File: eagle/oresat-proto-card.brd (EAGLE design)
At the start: 99 x 95.3 mm, 99 parts, among them J1 J-SAMTEC-TFM-110-X1-XXX-D-RA, J2 U.FL, J3 U.FL, J4 U.FL, J6 J-SAMTEC-TFM-120-X1-XXX-D-RA, J7 1.27MM-SWD-CONNECTOR, Q3 MOSFET-PCH-SOT23-6, Q4 MOSFET-PCH-SOT23-6, Q5 PMV45EN, Q6 PMV45EN, U2 TCAN330, U3 MAX7310, U4 MAX4211, U5 TPS62111, U6 STM32F042K6, X1 16MHZ-2.5x2mm

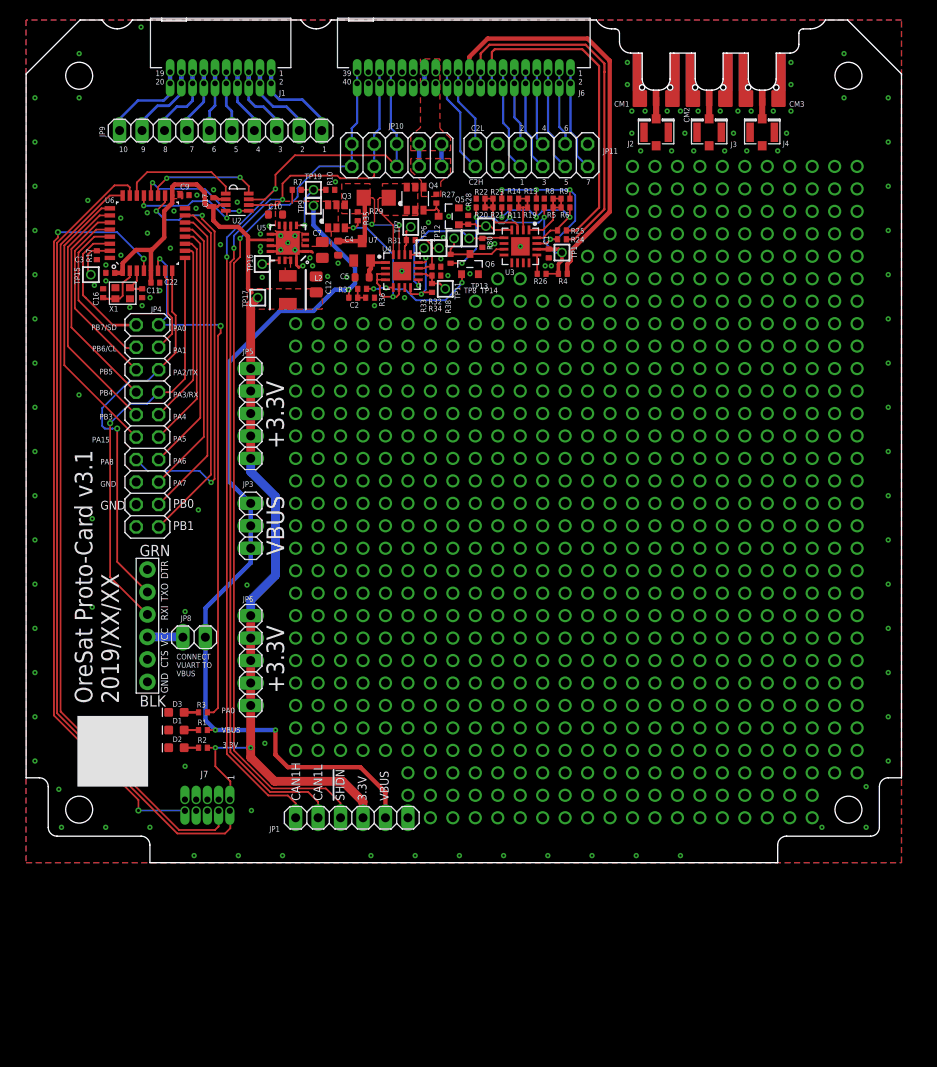
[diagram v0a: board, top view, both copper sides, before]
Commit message: More schematic and board polishing. Went over ERCs and DRCs, some layout polishing, more ground stitching.
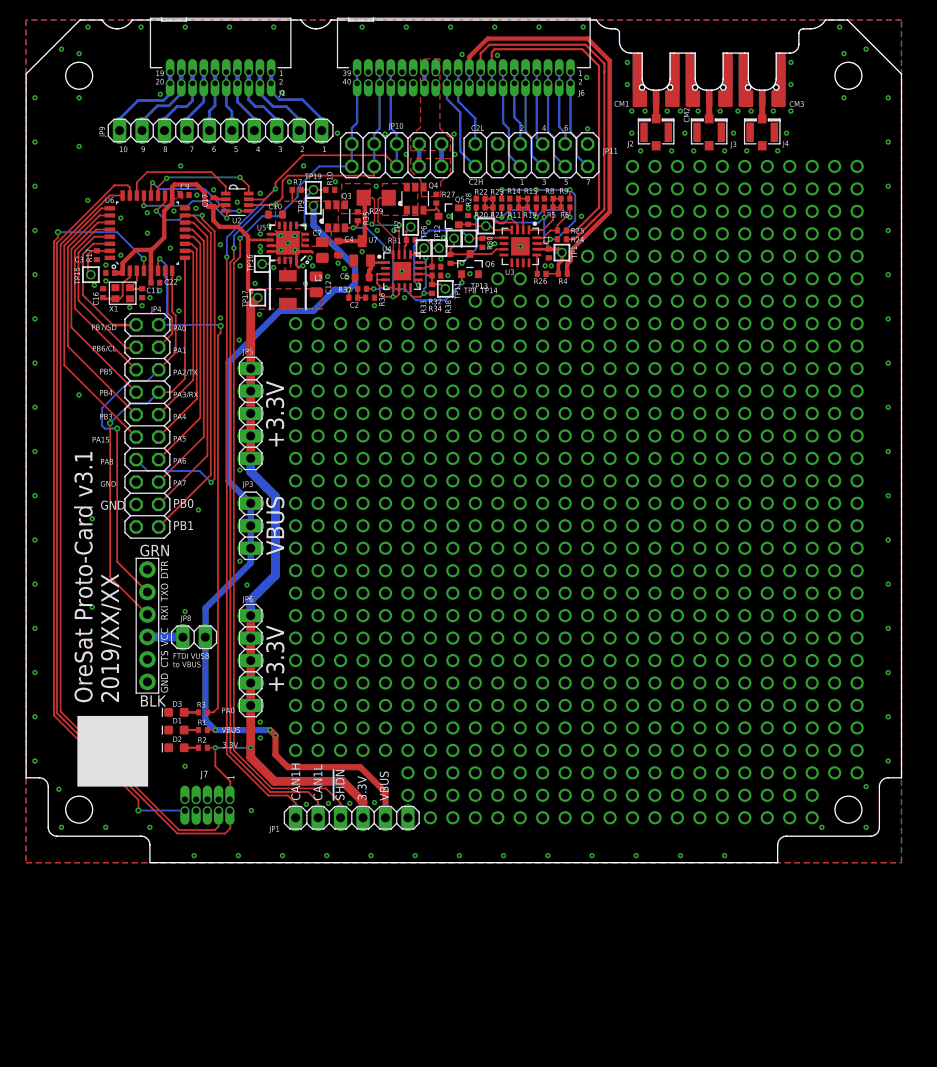
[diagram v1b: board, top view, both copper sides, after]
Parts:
- moved R33 0.10 mm to (45.9, 64.9)
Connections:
- net N$585 renamed MAX4211-3V3
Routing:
- net CAN1_L: track 108.7 -> 107.4 mm
- net CAN1_H: track 109.1 -> 108.6 mm
- net VBUSP: track 104.1 -> 104.6 mm, vias 3 -> 4
- net GND: vias 236 -> 288
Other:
- board text added: "FTDI VUSB to VBUS"
- board text removed: "CONNECT VUART TO VBUS"

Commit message: More board and schematic polishing. Swapped SWD connector with SMT version for easy removal. Added more test points on the MAX7210 power domain controller.
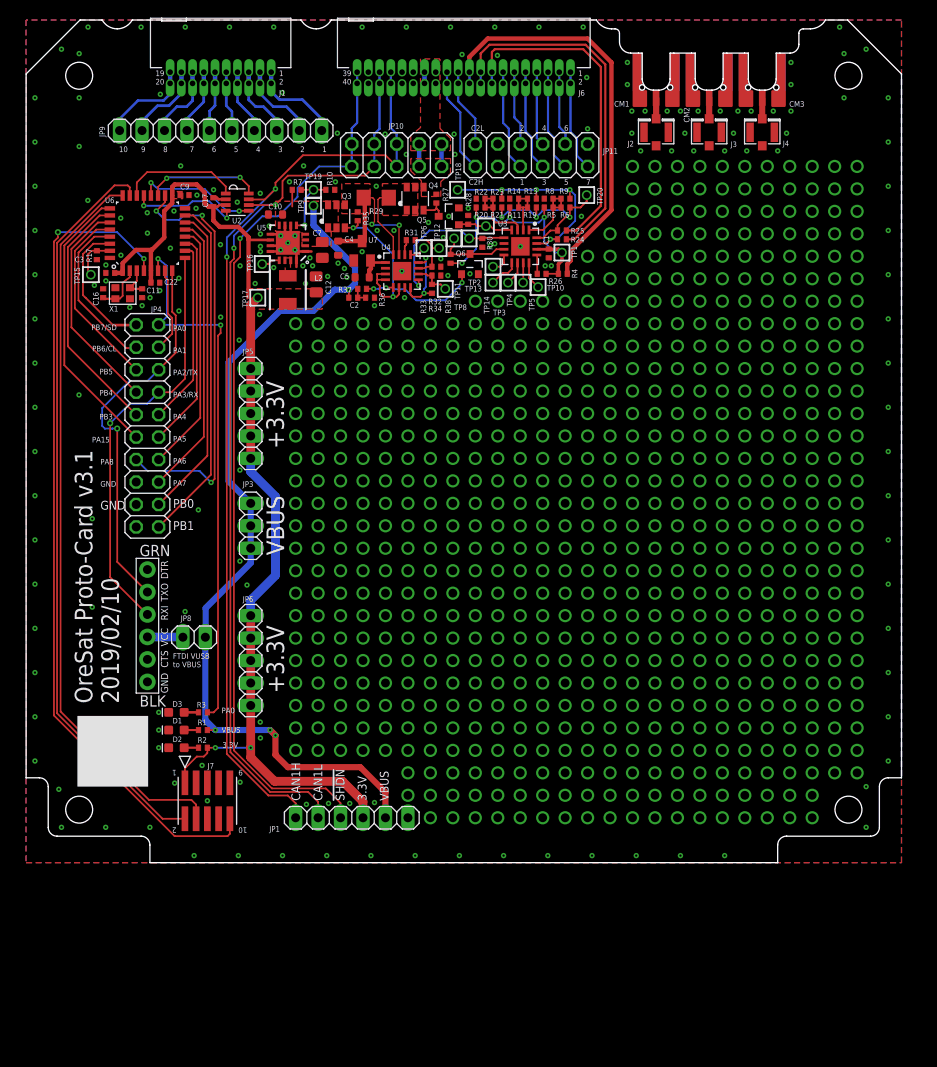
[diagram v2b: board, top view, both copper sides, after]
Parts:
- removed TP7: TEST-POINT, Tova:2MM-TEST-POINT
- added TP10, TP18, TP2, TP20, TP3, TP4, TP5: TEST-POINT, Tova:2MM-TEST-POINT
- J7: value 1.27MM-SWD-CONNECTOR -> FTSH-105-XX-X-DV-K; device J-CNC-3220-10-0100-00-ARM-SWD-port:1.27MM_2X5 -> J-Samtec-FTSH-105-XXX-DV-K-ARM-SWD:CON10_2X5_DUK_FTSH
- moved J7 0.50 mm to (20.5, 7.00), turned to 180 degrees
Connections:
- new net N$480: TP2.1, U3.8
- new net N$482: TP3.1, U3.9
- new net N$518: TP4.1, U3.10
- new net N$523: TP5.1, U3.11
- new net N$573: TP10.1, U3.12
- net 3.3V: now also J7.1; no longer J7.VTREF
- net GND: now also J7.3, J7.5, J7.9; no longer J7.GND, J7.GND@2, J7.GNDDET
- net N$598: no longer TP7.1
- net NRESET: now also J7.10; no longer J7.!RESET
- net PEN-SCL-FILT: now also TP18.1
- net PEN-SDA-FILT: now also TP20.1
- net SWCLK: now also J7.4; no longer J7.SWDCLK
- net SWDIO: now also J7.2; no longer J7.SWDIO
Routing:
- net SWDIO: track 92.6 -> 84.5 mm
- net NRESET: track 87.1 -> 94.5 mm, vias 3 -> 2
- net PEN-SCL-FILT: track 20.7 -> 25.7 mm
- net SWCLK: track 87.5 -> 83.4 mm
- net N$482: track 0.00 -> 3.47 mm, vias 1 -> 0
- net N$573: track 0.00 -> 3.16 mm
- net PEN-SDA-FILT: track 17.6 -> 20.3 mm
- net N$518: track 0.00 -> 2.69 mm
- net N$480: track 0.00 -> 2.31 mm
- net N$523: track 0.00 -> 2.25 mm
- net N$598: track 3.42 -> 1.71 mm
- net GND: track 18.2 -> 17.4 mm, vias 288 -> 295
- net 3.3V: track 123.7 -> 122.9 mm
- net CAN1_L: track 107.4 -> 106.8 mm
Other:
- board text added: "2019/02/10"
- board text removed: "2019/XX/XX"

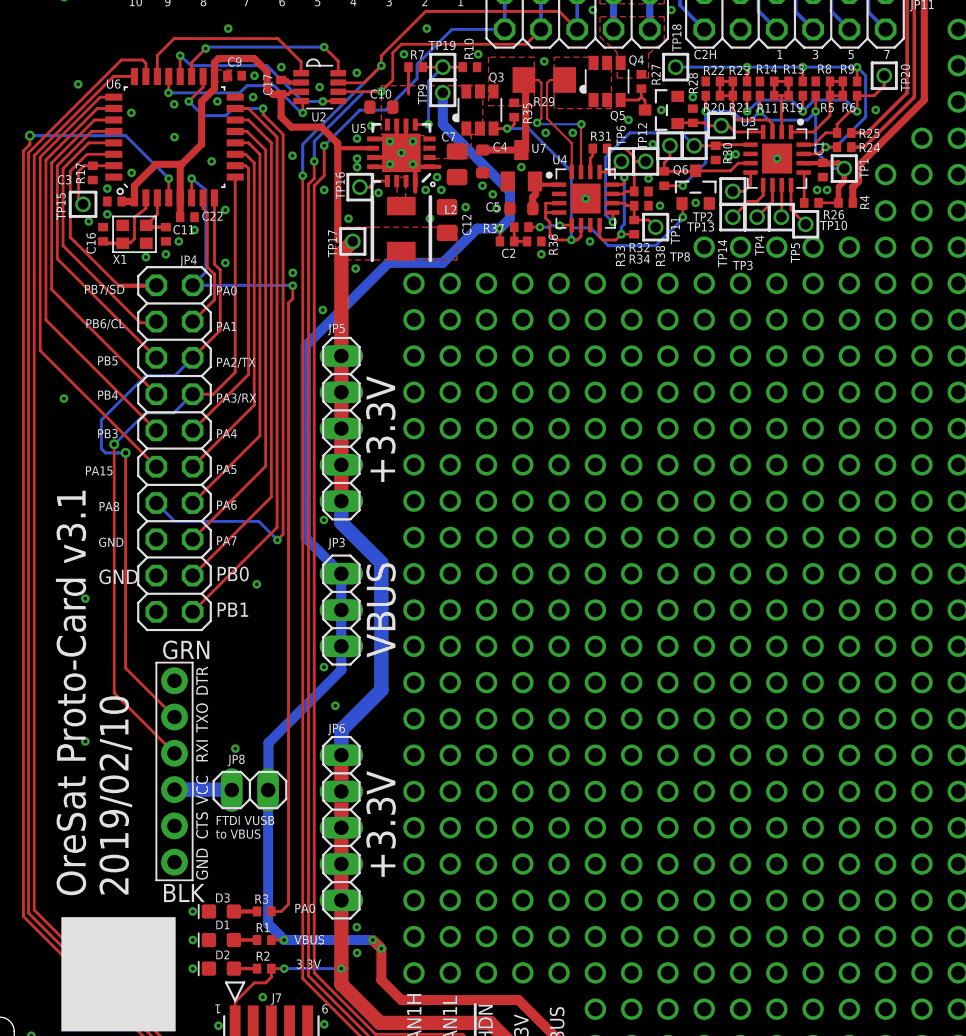
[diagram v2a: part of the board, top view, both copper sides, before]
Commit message: Latest OreSat protocard, version 3.1, with updated BOM, and design notes!
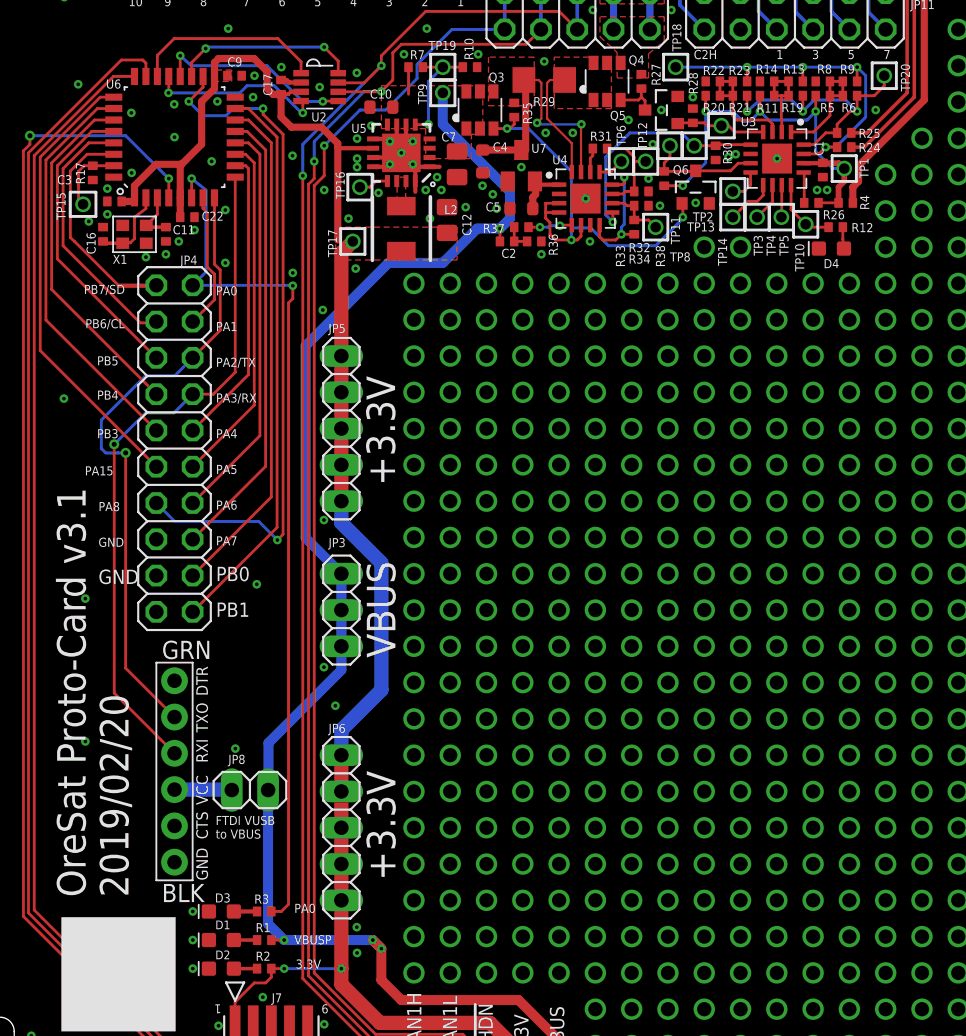
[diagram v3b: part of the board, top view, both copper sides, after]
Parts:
- added D4: AMBER, SparkFun-LED:LED-0603
- added R12: 2.7k, rcl_custom:.0402-B-NOSILK
- C2, R32, R34, R36, R37: value TBD -> NP
- D3: value GREEN -> AMBER
- R24, R25, R4: value TBD -> 100
- R26, R27, R28, R30, R35, R38: value 10K -> 10k
- R29: value (none) -> 100m
- R31, R33: value TBD -> 0
- U3: value MAX7310 -> MAX7310ATE
- U4: value MAX4211 -> MAX4211CETE
- U5: value TPS62111 -> TPS62111RSA
- U7: value (none) -> MCP1703A
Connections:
- new net N$575: D4.A, R12.1
- net CAN2_H: now also J6.21, J6.22, JP11.11; no longer J6.23, J6.24, JP11.12
- net CAN2_L: now also J6.23, J6.24, JP11.12; no longer J6.21, J6.22, JP11.11
- net GND: now also D4.C
- net N$573: now also R12.2
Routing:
- net CAN2_L: track 8.93 -> 12.0 mm
- net CAN2_H: track 12.0 -> 8.93 mm
- net N$573: track 3.16 -> 4.96 mm
- net N$575: track 0.00 -> 1.50 mm
- net GND: vias 295 -> 292
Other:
- board text added: "2019/02/20"
- board text added: "VBUSP"
- board text removed: "2019/02/10"
